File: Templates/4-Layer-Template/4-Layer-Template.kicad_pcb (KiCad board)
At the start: 4 copper layers, 0 parts

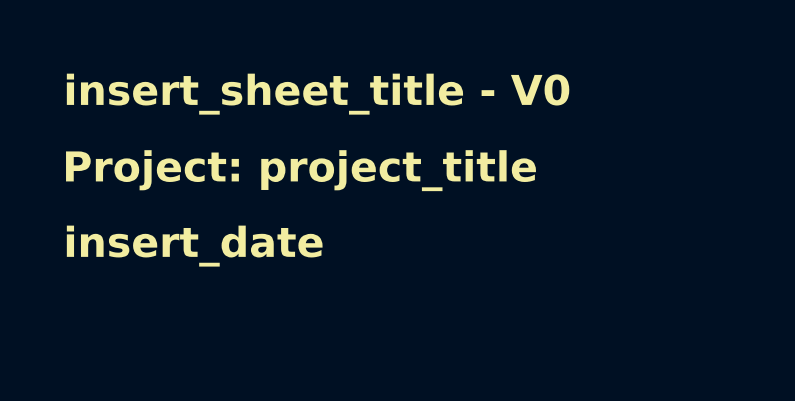
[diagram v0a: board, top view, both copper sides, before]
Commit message: Fixed template silkscreen
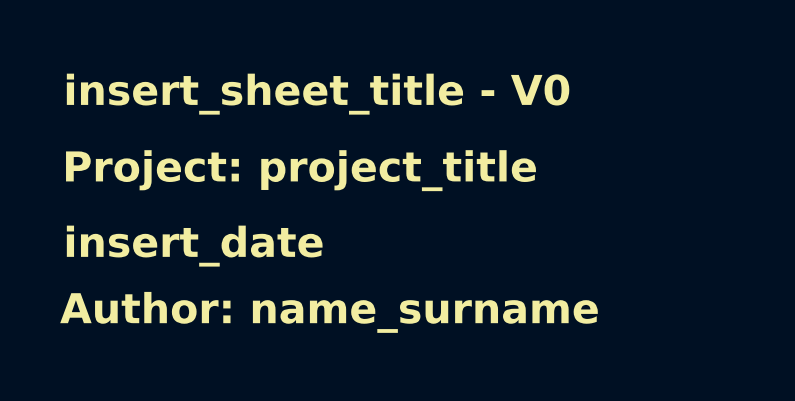
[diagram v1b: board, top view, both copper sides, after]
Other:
- board text added: "${COMMENT2}"
